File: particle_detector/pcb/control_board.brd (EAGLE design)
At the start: 51 x 32 mm, 29 parts, among them IC1 LT1807R, IC3 LT3461, IC4 TEENSY 3.2

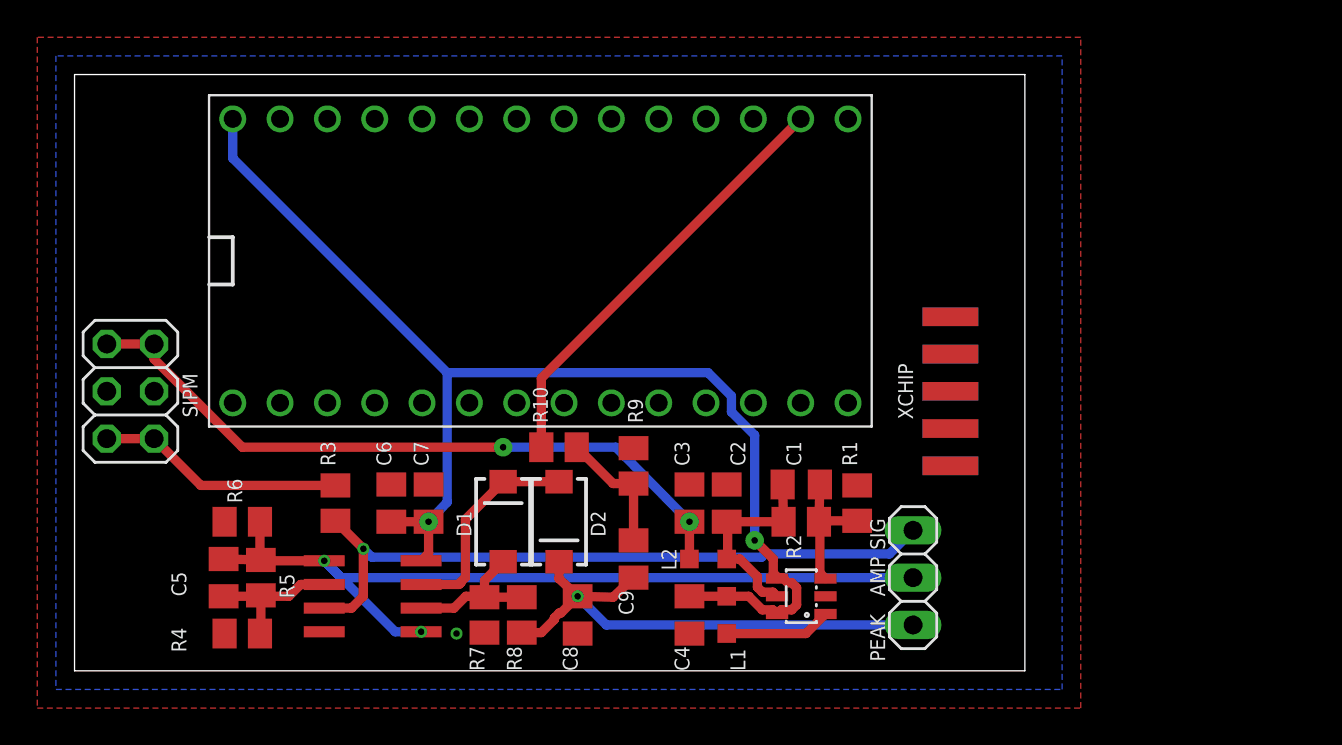
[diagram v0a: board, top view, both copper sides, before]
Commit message: update EDA with xinabox footprint; board done, awaiting fabhouse confirmation
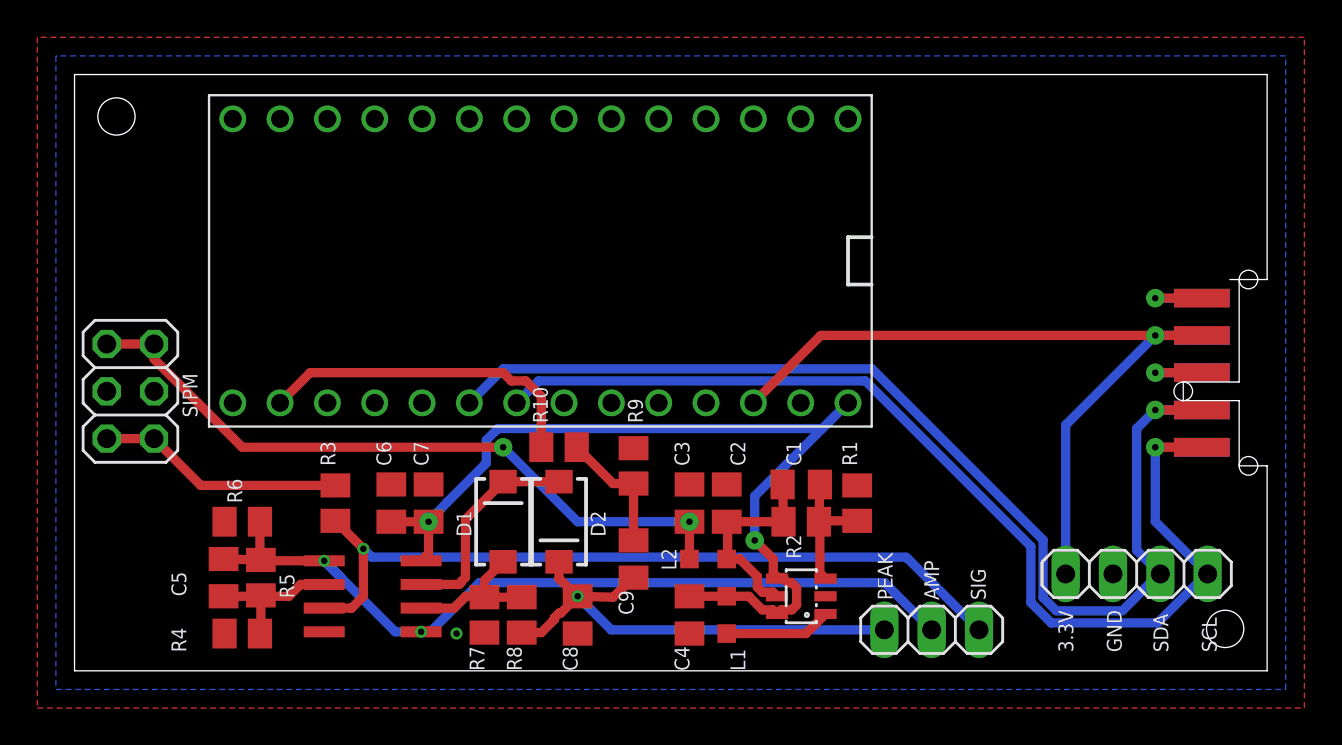
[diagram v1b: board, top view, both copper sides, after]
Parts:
- removed XCHIP: (no value), personal:1X05_PAD
- added I2C: (no value), pinhead:1X04
- added XBUS: (no value), personal:XBUS_1X05_PAD
- moved TOUCH 2.97 mm to (72.0, 2.20), turned to 180 degrees
- turned IC4 to 270 degrees
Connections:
- new net VBAT: XBUS.P5B, XBUS.P5T
- net 3.3V: now also I2C.4, XBUS.P4B, XBUS.P4T
- net GND: now also I2C.3, XBUS.P3B, XBUS.P3T
- net SCL: now also I2C.1, XBUS.P1B, XBUS.P1T
- net SDA: now also I2C.2, XBUS.P2B, XBUS.P2T
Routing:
- net SDA: track 0.00 -> 60.6 mm, vias 0 -> 1
- net SCL: track 0.00 -> 58.8 mm, vias 0 -> 1
- net 3.3V: track 0.00 -> 42.9 mm, vias 0 -> 1
- net VCC: track 66.2 -> 48.7 mm
- net N$10: track 23.4 -> 17.9 mm
- net VBAT: track 0.00 -> 5.00 mm, vias 0 -> 1
- net GND: track 0.00 -> 5.00 mm, vias 1 -> 2
- net SIG_RAW: track 37.3 -> 41.9 mm
- net SIG_PEAK: track 28.2 -> 26.8 mm
- net SIG_AMP: track 46.2 -> 45.1 mm
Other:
- board size 51 x 32 mm -> 64 x 32 mm
- board text added: "3.3V"
- board text added: "GND"
- board text added: "SCL"
- board text added: "SDA"
